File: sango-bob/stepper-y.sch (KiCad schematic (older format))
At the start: 26 parts, among them P701 CONN_8, P702 CONN_8, P703 MOT_Y, U701 A4985-LP

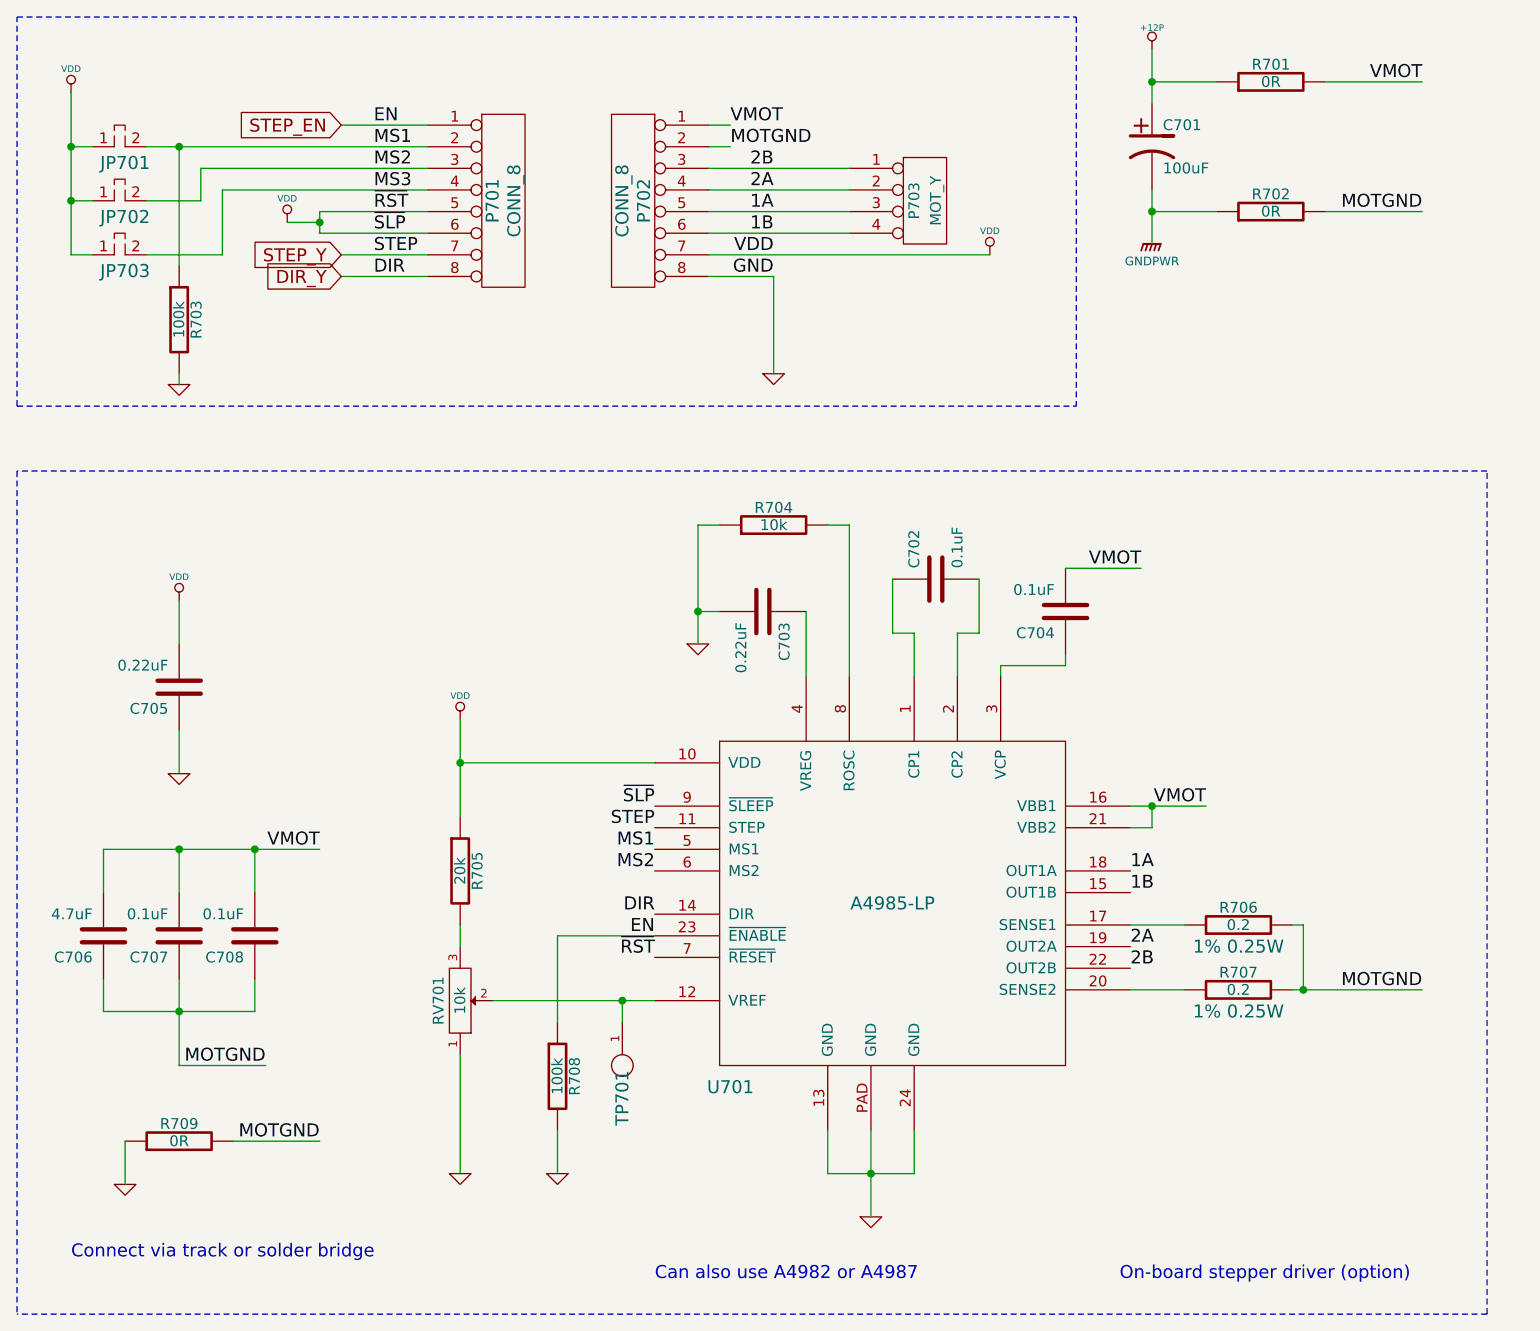
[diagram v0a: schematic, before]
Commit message: Updates to symbols and fix some ERC errors
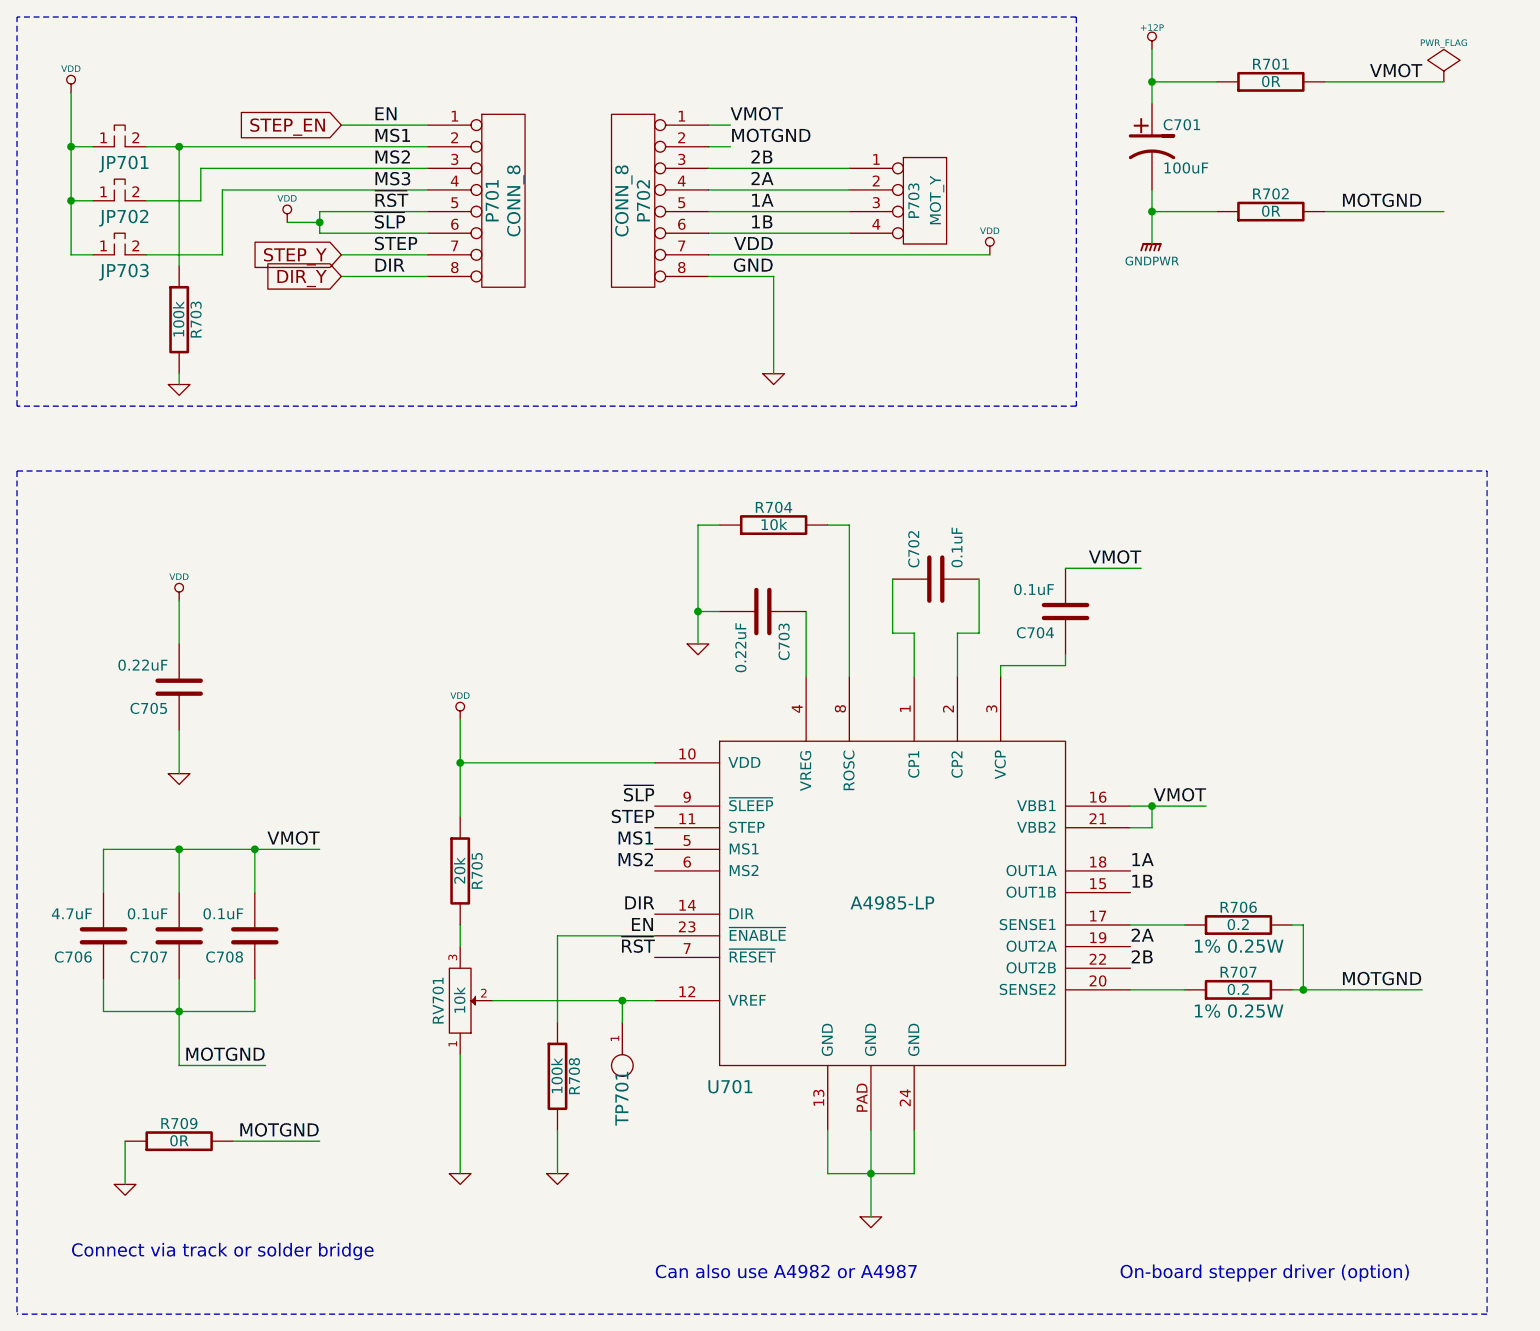
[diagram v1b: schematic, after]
